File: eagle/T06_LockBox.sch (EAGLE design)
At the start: 29 parts, among them T1 2N3904, T2 2N3904, T3 2N3904

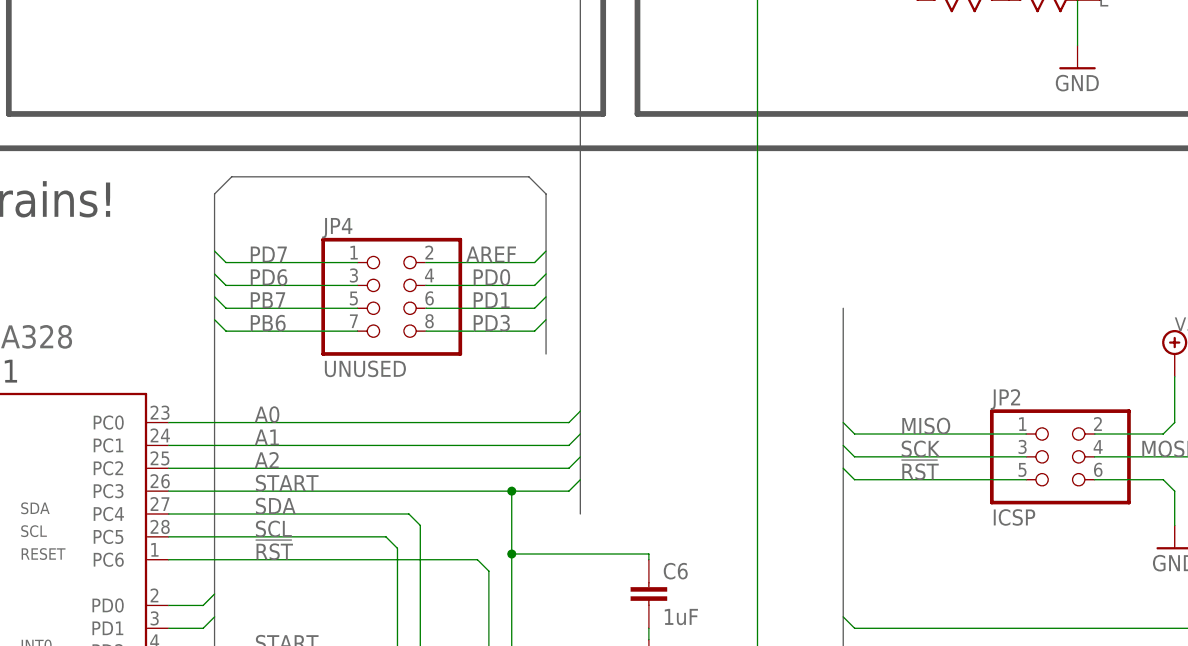
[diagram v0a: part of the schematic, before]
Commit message: Added 2x5 pin headder and pull up resistor to the ATMEGA reset line.
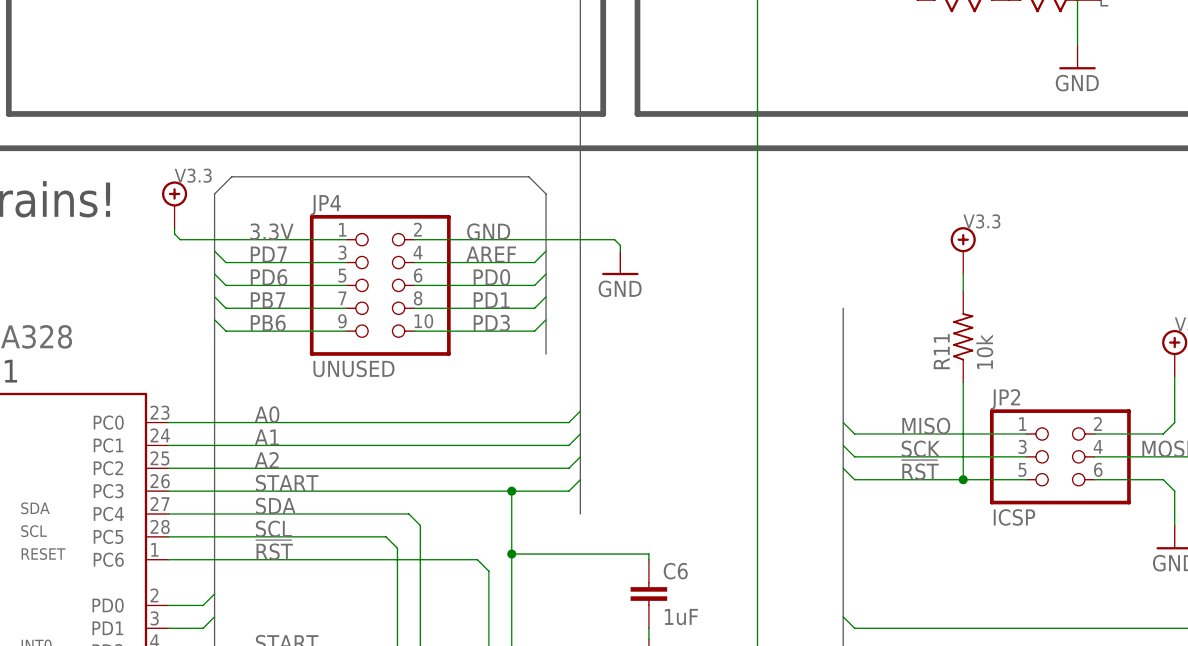
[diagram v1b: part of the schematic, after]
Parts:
- added R11: 10k, T06_Lockbox:R-US_M0805
- JP4: device T06_Lockbox:PINHD-2X4 -> T06_Lockbox:PINHD-2X5
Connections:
- net !RST: now also R11.1
- net 3.3V: now also JP4.1, R11.2
- net AREF: now also JP4.4; no longer JP4.2
- net GND: now also JP4.2
- net PB6: now also JP4.9; no longer JP4.7
- net PB7: now also JP4.7; no longer JP4.5
- net PD0: now also JP4.6; no longer JP4.4
- net PD1: now also JP4.8; no longer JP4.6
- net PD3: now also JP4.10; no longer JP4.8
- net PD6: now also JP4.5; no longer JP4.3
- net PD7: now also JP4.3; no longer JP4.1
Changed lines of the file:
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@@
 <?xml version="1.0" encoding="utf-8"?>
 <!DOCTYPE eagle SYSTEM "eagle.dtd">
-<eagle version="6.5.0">
+<eagle version="7.1.0">
 <drawing>
 <settings>
@@
 <setting verticaltext="up"/>
 </settings>
-<grid distance="0.1" unitdist="inch" unit="inch" style="lines" multiple="1" display="no" altdistance="0.01" altunitdist="inch" altunit="inch"/>
+<grid distance="0.025" unitdist="inch" unit="inch" style="lines" multiple="1" display="yes" altdistance="0.01" altunitdist="inch" altunit="inch"/>
 <layers>
 <layer number="1" name="Top" color="4" fill="1" visible="no" active="no"/>
@@
 <part name="C4" library="T06_Lockbox" deviceset="C" device="C1206" value="10uF"/>
 <part name="C5" library="T06_Lockbox" deviceset="C" device="" value="1uF"/>
-<part name="JP4" library="T06_Lockbox" deviceset="PINHD-2X4" device="" value="UNUSED"/>
+<part name="JP4" library="T06_Lockbox" deviceset="PINHD-2X5" device="" value="UNUSED"/>
+<part name="GND2" library="T06_Lockbox" deviceset="GND" device=""/>
+<part name="V7" library="T06_Lockbox" deviceset="V3.3" device=""/>
+<part name="R11" library="T06_Lockbox" deviceset="R-US_" device="M0805" value="10k"/>
+<part name="V8" library="T06_Lockbox" deviceset="V3.3" device=""/>
 </parts>
 <sheets>
@@
 <instance part="C4" gate="G$1" x="25.4" y="143.51"/>
 <instance part="C5" gate="G$1" x="35.56" y="143.51"/>
-<instance part="JP4" gate="A" x="135.255" y="97.79"/>
+<instance part="JP4" gate="A" x="133.985" y="100.33"/>
+<instance part="GND2" gate="1" x="161.925" y="101.6"/>
+<instance part="V7" gate="G1" x="112.395" y="109.22"/>
+<instance part="R11" gate="G$1" x="200.025" y="94.615" rot="R90"/>
+<instance part="V8" gate="G1" x="200.025" y="104.14"/>
 </instances>
 <busses>
@@
 <wire x1="38.1" y1="100.33" x2="36.83" y2="100.33" width="0.1524" layer="91"/>
 </segment>
+<segment>
+<pinref part="JP4" gate="A" pin="2"/>
+<wire x1="139.065" y1="105.41" x2="161.29" y2="105.41" width="0.1524" layer="91"/>
+<wire x1="161.29" y1="105.41" x2="161.925" y2="104.775" width="0.1524" layer="91"/>
+<wire x1="161.925" y1="104.775" x2="161.925" y2="104.14" width="0.1524" layer="91"/>
+<pinref part="GND2" gate="1" pin="GND"/>
+<label x="144.78" y="105.41" size="1.778" layer="95"/>
+</segment>
 </net>
 <net name="SDA" class="0">
@@
 <wire x1="186.69" y1="80.01" x2="187.96" y2="78.74" width="0.1524" layer="91"/>
 <pinref part="JP2" gate="A" pin="5"/>
-<wire x1="187.96" y1="78.74" x2="207.01" y2="78.74" width="0.1524" layer="91"/>
+<wire x1="187.96" y1="78.74" x2="200.025" y2="78.74" width="0.1524" layer="91"/>
 <label x="193.04" y="78.74" size="1.778" layer="95"/>
+<junction x="200.025" y="78.74"/>
+<wire x1="200.025" y1="78.74" x2="207.01" y2="78.74" width="0.1524" layer="91"/>
+<pinref part="R11" gate="G$1" pin="1"/>
+<wire x1="200.025" y1="78.74" x2="200.025" y2="89.535" width="0.1524" layer="91"/>
 </segment>
 </net>
@@
 <wire x1="121.92" y1="33.02" x2="121.92" y2="34.29" width="0.1524" layer="91"/>
 </segment>
+<segment>
+<pinref part="JP4" gate="A" pin="1"/>
+<wire x1="131.445" y1="105.41" x2="113.03" y2="105.41" width="0.1524" layer="91"/>
+<wire x1="113.03" y1="105.41" x2="112.395" y2="106.045" width="0.1524" layer="91"/>
+<wire x1="112.395" y1="106.045" x2="112.395" y2="106.68" width="0.1524" layer="91"/>
+<pinref part="V7" gate="G1" pin="3.3V"/>
+<label x="120.65" y="105.41" size="1.778" layer="95"/>
+</segment>
+<segment>
+<pinref part="R11" gate="G$1" pin="2"/>
+<wire x1="200.025" y1="99.695" x2="200.025" y2="101.6" width="0.1524" layer="91"/>
+<pinref part="V8" gate="G1" pin="3.3V"/>
+</segment>
 </net>
 <net name="RED" class="0">
@@
 <segment>
 <wire x1="116.84" y1="96.52" x2="118.11" y2="95.25" width="0.1524" layer="91"/>
-<pinref part="JP4" gate="A" pin="7"/>
-<wire x1="118.11" y1="95.25" x2="132.715" y2="95.25" width="0.1524" layer="91"/>
 <label x="120.65" y="95.25" size="1.778" layer="95"/>
+<pinref part="JP4" gate="A" pin="9"/>
+<wire x1="118.11" y1="95.25" x2="131.445" y2="95.25" width="0.1524" layer="91"/>
 </segment>
 </net>
@@
 <segment>
 <wire x1="116.84" y1="99.06" x2="118.11" y2="97.79" width="0.1524" layer="91"/>
-<pinref part="JP4" gate="A" pin="5"/>
-<wire x1="118.11" y1="97.79" x2="132.715" y2="97.79" width="0.1524" layer="91"/>
 <label x="120.65" y="97.79" size="1.778" layer="95"/>
+<pinref part="JP4" gate="A" pin="7"/>
+<wire x1="118.11" y1="97.79" x2="131.445" y2="97.79" width="0.1524" layer="91"/>
 </segment>
 </net>
@@
 <segment>
 <wire x1="153.67" y1="104.14" x2="152.4" y2="102.87" width="0.1524" layer="91"/>
-<pinref part="JP4" gate="A" pin="2"/>
-<wire x1="152.4" y1="102.87" x2="140.335" y2="102.87" width="0.1524" layer="91"/>
 <label x="144.78" y="102.87" size="1.778" layer="95"/>
+<pinref part="JP4" gate="A" pin="4"/>
+<wire x1="152.4" y1="102.87" x2="139.065" y2="102.87" width="0.1524" layer="91"/>
 </segment>
 </net>
@@
 <segment>
 <wire x1="116.84" y1="104.14" x2="118.11" y2="102.87" width="0.1524" layer="91"/>
-<pinref part="JP4" gate="A" pin="1"/>
-<wire x1="118.11" y1="102.87" x2="132.715" y2="102.87" width="0.1524" layer="91"/>
 <label x="120.65" y="102.87" size="1.778" layer="95"/>
+<pinref part="JP4" gate="A" pin="3"/>
+<wire x1="118.11" y1="102.87" x2="131.445" y2="102.87" width="0.1524" layer="91"/>
 </segment>
 </net>
@@
 <segment>
 <wire x1="116.84" y1="101.6" x2="118.11" y2="100.33" width="0.1524" layer="91"/>
-<pinref part="JP4" gate="A" pin="3"/>
-<wire x1="118.11" y1="100.33" x2="132.715" y2="100.33" width="0.1524" layer="91"/>
 <label x="120.65" y="100.33" size="1.778" layer="95"/>
+<pinref part="JP4" gate="A" pin="5"/>
+<wire x1="118.11" y1="100.33" x2="131.445" y2="100.33" width="0.1524" layer="91"/>
 </segment>
 </net>
@@
 <segment>
 <wire x1="153.67" y1="96.52" x2="152.4" y2="95.25" width="0.1524" layer="91"/>
-<pinref part="JP4" gate="A" pin="8"/>
-<wire x1="152.4" y1="95.25" x2="140.335" y2="95.25" width="0.1524" layer="91"/>
 <label x="145.415" y="95.25" size="1.778" layer="95"/>
+<pinref part="JP4" gate="A" pin="10"/>
+<wire x1="152.4" y1="95.25" x2="139.065" y2="95.25" width="0.1524" layer="91"/>
 </segment>
 </net>
@@
 <segment>
 <wire x1="153.67" y1="101.6" x2="152.4" y2="100.33" width="0.1524" layer="91"/>
-<pinref part="JP4" gate="A" pin="4"/>
-<wire x1="152.4" y1="100.33" x2="140.335" y2="100.33" width="0.1524" layer="91"/>
 <label x="145.415" y="100.33" size="1.778" layer="95"/>
+<pinref part="JP4" gate="A" pin="6"/>
+<wire x1="152.4" y1="100.33" x2="139.065" y2="100.33" width="0.1524" layer="91"/>
 </segment>
 </net>
@@
 <segment>
 <wire x1="153.67" y1="99.06" x2="152.4" y2="97.79" width="0.1524" layer="91"/>
-<pinref part="JP4" gate="A" pin="6"/>
-<wire x1="152.4" y1="97.79" x2="140.335" y2="97.79" width="0.1524" layer="91"/>
 <label x="145.415" y="97.79" size="1.778" layer="95"/>
-</segment>
-</net>
+<pinref part="JP4" gate="A" pin="8"/>
+<wire x1="152.4" y1="97.79" x2="139.065" y2="97.79" width="0.1524" layer="91"/>
+</segment>
+</net>
